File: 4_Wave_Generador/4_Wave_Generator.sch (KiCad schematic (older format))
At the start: 131 parts, among them J10 Jumper, J11 Jumper, J12 Jumper, J13 Jumper, J14 Jumper, J15 Jumper, J4 RESET, J5 Jumper, J6 Jumper, J7 Jumper, J8 Jumper, P1 ECG INPUTS, P10 INPUT_ADC_PIC, P11 DIG_ATMEGA, P12 RG_8421, P13 OUTPUT_DIG_PIC, P14 OUTPUT_TARJET, P15 MUX_S1, P16 DIG_MICRO, P17 SUPPLY_-12V, P18 RS232, P19 I2C, P2 PIC_PROGRAMER, P20 DIG_ATMEGA2, P3 SPI_MICRO, P31 TORNILLO, P32 TORNILLO, P33 TORNILLO, P34 TORNILLO, P35 RS232_PIC, P4 AD8232_CONTROL, P5 OXIMETRO, P6 SUPPLY_12V, P7 SUPPLY_VDD, P8 MCLK_EXTERNAL, P9 SPI_AD9833, SW1 SW_Push, SW2 RESET_PIC, U1 PIC16F688, U2 AD8232_A, U3 ATMEGA328P-AU_MIO, U4 AD9833, U5 LD1117S33TR_MIO, U6 ADG819, U7 ADG819, U8 AD8421, U9 ADG819, Y1 Crystal_8MHz, Y2 XRCHA_16M

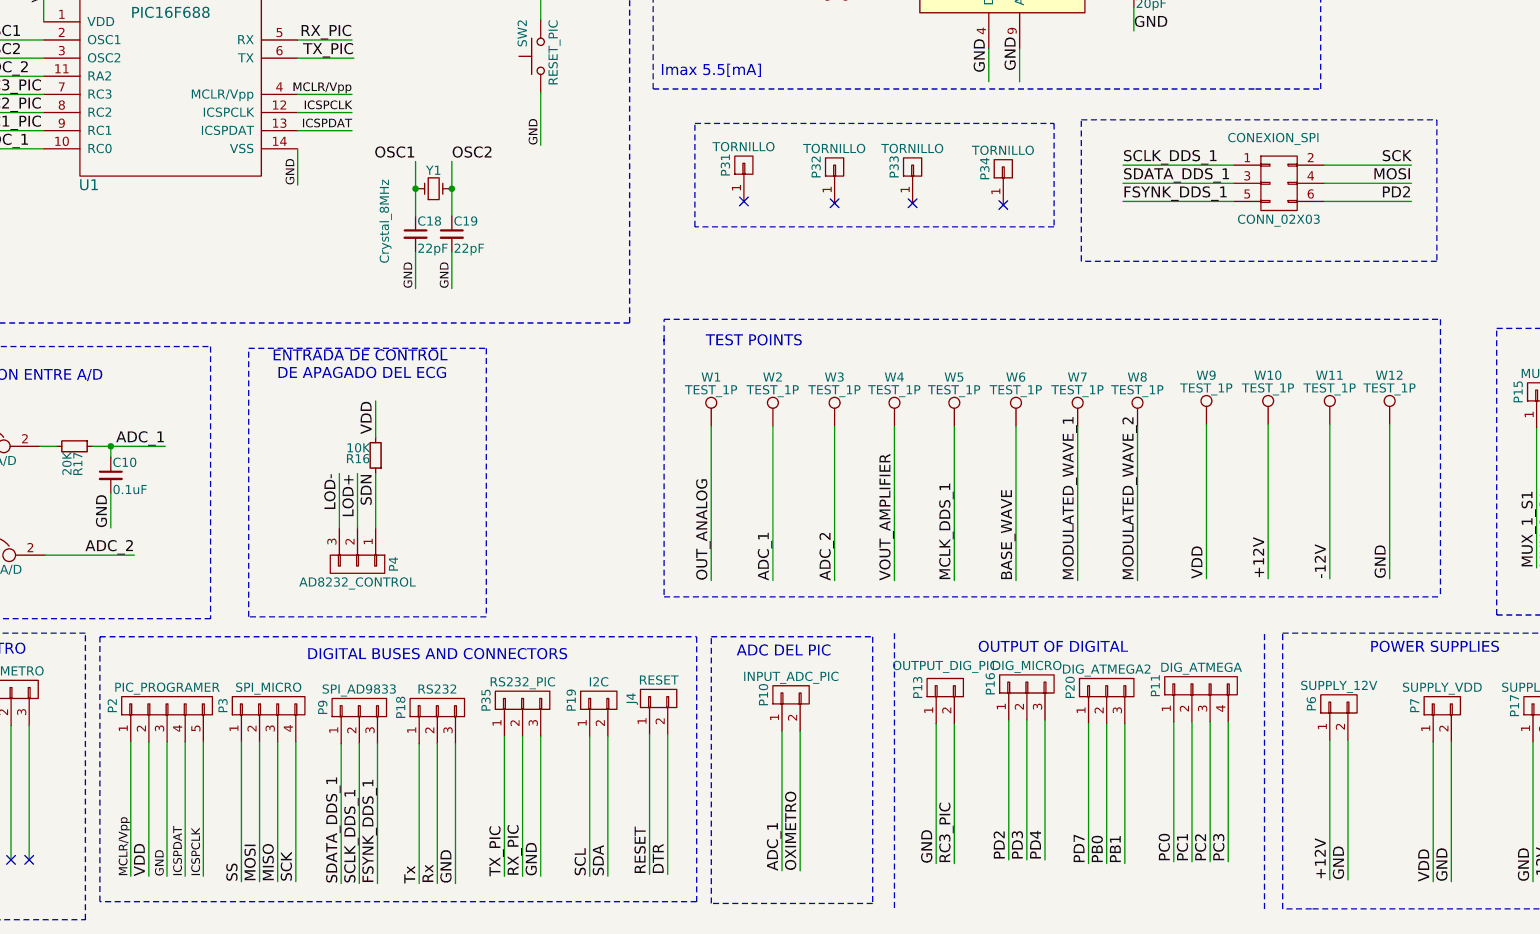
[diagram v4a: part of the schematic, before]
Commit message: GENERADOR V11
TRAZADO DE PISTAS Y VIAS
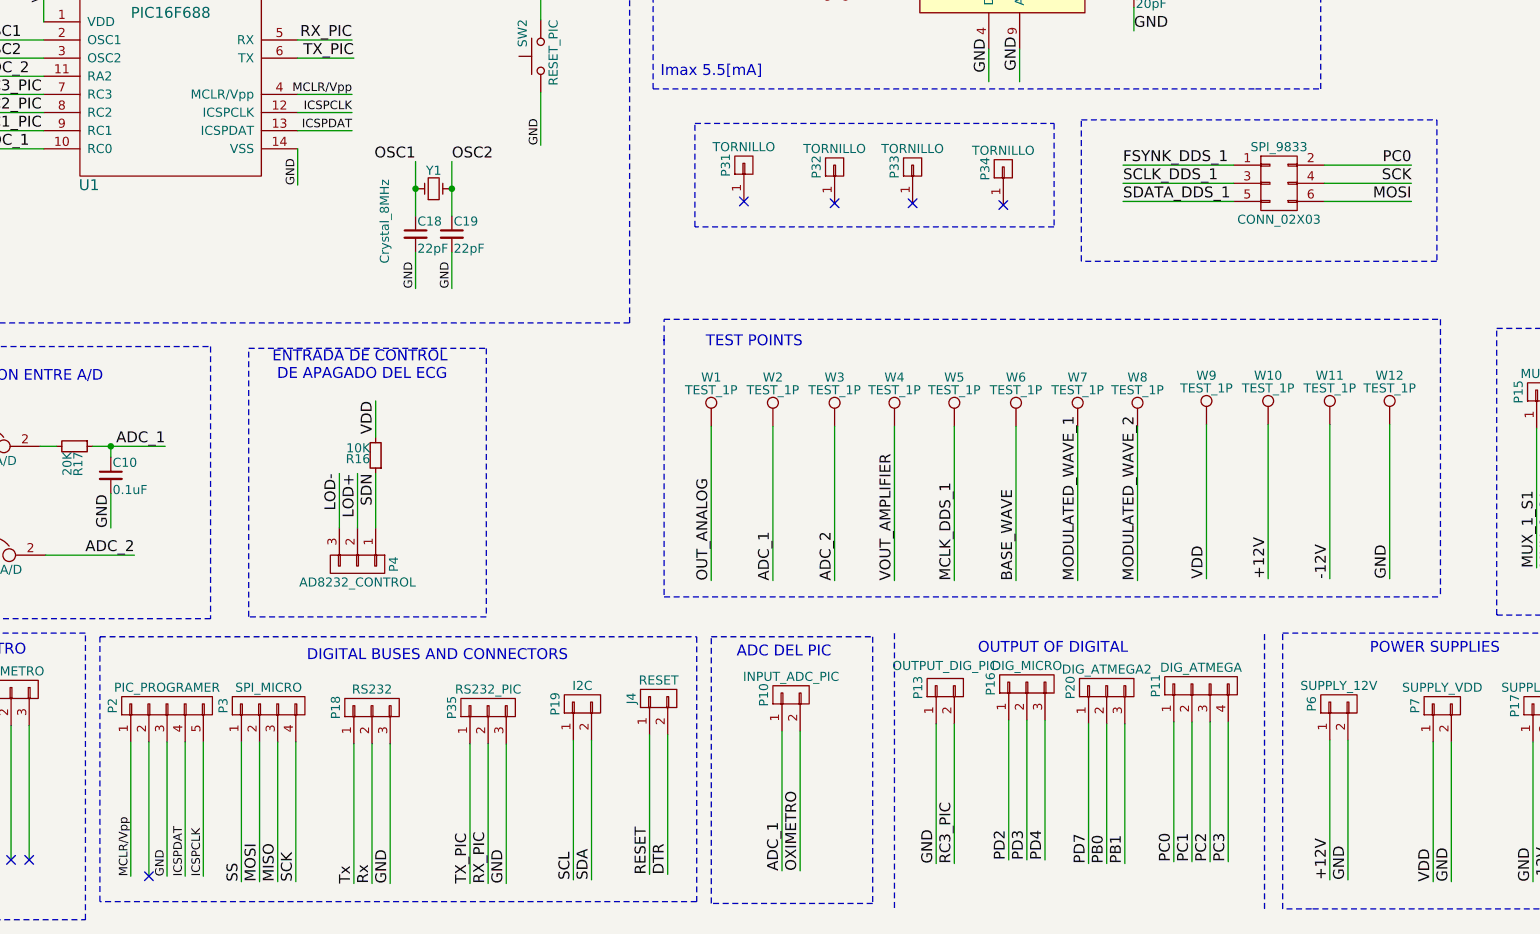
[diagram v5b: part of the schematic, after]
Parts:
- removed CONEXION_SPI: CONN_02X03, Pin_Headers:Pin_Header_Straight_2x03_Pitch2.54mm, symbol CONN_02X03
- removed P9: SPI_AD9833, Foot_Prints_Manager_Outputs:SPI_AD9833, symbol CONN_01X03
- added SPI_9833: CONN_02X03, Foot_Prints_Manager_Outputs:SPI_9833, symbol CONN_02X03
- U5: footprint TO_SOT_Packages_SMD:SOT-223 -> Foot_Prints_Manager_Outputs:SOT-223_este
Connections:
- net FSYNK_DDS_1: now also SPI_9833.1 (P1)
- net MOSI: now also SPI_9833.6 (P6)
- net PC0: now also SPI_9833.2 (P2)
- net SCK: now also SPI_9833.4 (P4)
- net SCLK_DDS_1: now also SPI_9833.3 (P3)
- net SDATA_DDS_1: now also SPI_9833.5 (P5)
- net VDD: no longer P2.2 (P2)
- no-connect marks 15 -> 16
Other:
- moved on the sheet: P18, P19, P35
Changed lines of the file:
@@
 Text Label 3120 10970 1    60   ~ 0
 SCK
-Text Label 3900 10980 1    60   ~ 0
+Text Label 3540 10980 1    60   ~ 0
 Rx
-Text Label 3800 10980 1    60   ~ 0
+Text Label 3440 10980 1    60   ~ 0
 Tx
-Text Label 4000 10980 1    60   ~ 0
+Text Label 3640 10980 1    60   ~ 0
 GND
 Text Notes 3180 9760 0    60   ~ 0
@@
 	0    -1   -1   0
 $EndComp
-Text Label 4840 10940 1    60   ~ 0
+Text Label 4750 10960 1    60   ~ 0
 SDA
-Text Label 4740 10940 1    60   ~ 0
+Text Label 4650 10960 1    60   ~ 0
 SCL
 $Comp
@@
 	1    0    0    -1
 $EndComp
-Text Label 2310 10940 1    60   ~ 0
-VDD
 $Comp
 L PASO_A/D JP1
@@
 Text Label 3440 6430 2    60   ~ 0
 TX_PIC
-Text Label 4270 10940 1    60   ~ 0
+Text Label 4080 10980 1    60   ~ 0
 TX_PIC
-Text Label 4370 10940 1    60   ~ 0
+Text Label 4180 10980 1    60   ~ 0
 RX_PIC
-Text Label 4470 10940 1    60   ~ 0
+Text Label 4280 10980 1    60   ~ 0
 GND
 Text Label 1380 6630 0    60   ~ 0
@@
 $EndComp
 $Comp
-L LD1117S33TR_MIO U5
-U 1 1 59D82649
-P 11050 1080
-F 0 "U5" H 11050 1330 50  0000 C CNN
-F 1 "LD1117S33TR_MIO" H 11050 1280 50  0000 C CNN
-F 2 "TO_SOT_Packages_SMD:SOT-223" H 11050 1180 50  0001 C CNN
-F 3 "" H 11050 1080 50  0001 C CNN
-	1    11050 1080
-	1    0    0    -1
-$EndComp
-$Comp
 L XRCHA_16M Y2
 U 1 1 59DAC6C5
@@
 	3120 10200 3120 10970
 Wire Wire Line
-	3800 10210 3800 10980
-Wire Wire Line
-	3900 10210 3900 10980
-Wire Wire Line
-	4000 10210 4000 10980
+	3440 10210 3440 10980
+Wire Wire Line
+	3540 10210 3540 10980
+Wire Wire Line
+	3640 10210 3640 10980
 Wire Notes Line
 	9700 550  9700 1620
@@
 	12660 2010 12660 550
 Wire Wire Line
-	4740 10170 4740 10940
-Wire Wire Line
-	4840 10170 4840 10940
+	4650 10190 4650 10960
+Wire Wire Line
+	4750 10190 4750 10960
 Wire Wire Line
 	11450 1030 12030 1030
@@
 	3130 6430 3440 6430
 Wire Wire Line
-	4270 10170 4270 10940
-Wire Wire Line
-	4370 10170 4370 10940
-Wire Wire Line
-	4470 10170 4470 10940
+	4080 10210 4080 10980
+Wire Wire Line
+	4180 10210 4180 10980
+Wire Wire Line
+	4280 10210 4280 10980
 Wire Wire Line
 	6650 10100 6650 10870
@@
 Text Notes 5550 9740 0    60   ~ 0
 ADC DEL PIC\n
-$Comp
-L CONN_01X03 P9
-U 1 1 59E0B7ED
-P 3470 10010
-F 0 "P9" H 3470 10210 50  0000 C CNN
-F 1 "SPI_AD9833" V 3570 10010 50  0000 C CNN
-F 2 "Foot_Prints_Manager_Outputs:SPI_AD9833" H 3470 10010 50  0001 C CNN
-F 3 "" H 3470 10010 50  0000 C CNN
-	1    3470 10010
-	0    -1   -1   0
-$EndComp
-Wire Wire Line
-	3370 10210 3370 10980
-Wire Wire Line
-	3470 10210 3470 10980
-Wire Wire Line
-	3570 10210 3570 10980
-Text Label 3370 10980 1    60   ~ 0
-SDATA_DDS_1
-Text Label 3470 10980 1    60   ~ 0
-SCLK_DDS_1
-Text Label 3570 10980 1    60   ~ 0
-FSYNK_DDS_1
 Text Label 6420 9310 1    60   ~ 0
 VOUT_AMPLIFIER
@@
 L CONN_01X03 P18
 U 1 1 59D5CB3B
-P 3900 10010
-F 0 "P18" H 3900 10210 50  0000 C CNN
-F 1 "RS232" V 4000 10010 50  0000 C CNN
-F 2 "Foot_Prints_Manager_Outputs:RS232" H 3900 10010 50  0001 C CNN
-F 3 "" H 3900 10010 50  0000 C CNN
-	1    3900 10010
+P 3540 10010
+F 0 "P18" H 3540 10210 50  0000 C CNN
+F 1 "RS232" V 3640 10010 50  0000 C CNN
+F 2 "Foot_Prints_Manager_Outputs:RS232" H 3540 10010 50  0001 C CNN
+F 3 "" H 3540 10010 50  0000 C CNN
+	1    3540 10010
 	0    -1   -1   0
 $EndComp
@@
 L CONN_01X02 P19
 U 1 1 59D6289E
-P 4790 9970
-F 0 "P19" H 4790 10120 50  0000 C CNN
-F 1 "I2C" V 4890 9970 50  0000 C CNN
-F 2 "Foot_Prints_Manager_Outputs:I2C_2X4" H 4790 9970 50  0001 C CNN
-F 3 "" H 4790 9970 50  0000 C CNN
-	1    4790 9970
+P 4700 9990
+F 0 "P19" H 4700 10140 50  0000 C CNN
+F 1 "I2C" V 4800 9990 50  0000 C CNN
+F 2 "Foot_Prints_Manager_Outputs:I2C_2X4" H 4700 9990 50  0001 C CNN
+F 3 "" H 4700 9990 50  0000 C CNN
+	1    4700 9990
 	0    -1   -1   0
 $EndComp
@@
 L CONN_01X03 P35
 U 1 1 59E4555A
-P 4370 9970
-F 0 "P35" H 4370 10170 50  0000 C CNN
-F 1 "RS232_PIC" V 4470 9970 50  0000 C CNN
-F 2 "Foot_Prints_Manager_Outputs:RS232" H 4370 9970 50  0001 C CNN
-F 3 "" H 4370 9970 50  0000 C CNN
-	1    4370 9970
+P 4180 10010
+F 0 "P35" H 4180 10210 50  0000 C CNN
+F 1 "RS232_PIC" V 4280 10010 50  0000 C CNN
+F 2 "Foot_Prints_Manager_Outputs:RS232" H 4180 10010 50  0001 C CNN
+F 3 "" H 4180 10010 50  0000 C CNN
+	1    4180 10010
 	0    -1   -1   0
 $EndComp
@@
 	0    -1   -1   0
 $EndComp
-$Comp
-L CONN_02X03 CONEXION_SPI
-U 1 1 59D69BA8
+Text Label 7680 7120 0    60   ~ 0
+SCLK_DDS_1
+Text Label 7680 7220 0    60   ~ 0
+SDATA_DDS_1
+Text Label 7680 7020 0    60   ~ 0
+FSYNK_DDS_1
+Wire Wire Line
+	7680 7020 8290 7020
+Wire Wire Line
+	7680 7120 8290 7120
+Wire Wire Line
+	7680 7220 8290 7220
+Wire Wire Line
+	8790 7020 9270 7020
+Wire Wire Line
+	8790 7120 9270 7120
+Wire Wire Line
+	8790 7220 9270 7220
+Text Label 9270 7220 2    60   ~ 0
+MOSI
+Text Label 9270 7120 2    60   ~ 0
+SCK
+Text Label 9270 7020 2    60   ~ 0
+PC0
+Wire Notes Line
+	7450 6770 9410 6770
+Wire Notes Line
+	9410 6770 9410 7550
+Wire Notes Line
+	9410 7550 7450 7550
+Wire Notes Line
+	7450 7550 7450 6770
+$Comp
+L CONN_02X03 SPI_9833
+U 1 1 59DB8D35
 P 8540 7120
-F 0 "CONEXION_SPI" H 8510 7370 50  0000 C CNN
+F 0 "SPI_9833" H 8540 7320 50  0000 C CNN
 F 1 "CONN_02X03" H 8540 6920 50  0000 C CNN
-F 2 "Pin_Headers:Pin_Header_Straight_2x03_Pitch2.54mm" H 8540 5920 50  0001 C CNN
+F 2 "Foot_Prints_Manager_Outputs:SPI_9833" H 8540 5920 50  0001 C CNN
 F 3 "" H 8540 5920 50  0000 C CNN
 	1    8540 7120
 	1    0    0    -1
 $EndComp
-Text Label 7680 7020 0    60   ~ 0
-SCLK_DDS_1
-Text Label 7680 7120 0    60   ~ 0
-SDATA_DDS_1
-Text Label 7680 7220 0    60   ~ 0
-FSYNK_DDS_1
-Wire Wire Line
-	7680 7020 8290 7020
-Wire Wire Line
-	7680 7120 8290 7120
-Wire Wire Line
-	7680 7220 8290 7220
-Wire Wire Line
-	8790 7020 9270 7020
-Wire Wire Line
-	8790 7120 9270 7120
-Wire Wire Line
-	8790 7220 9270 7220
-Text Label 9270 7120 2    60   ~ 0
-MOSI
-Text Label 9270 7020 2    60   ~ 0
-SCK
-Text Label 9270 7220 2    60   ~ 0
-PD2
-Wire Notes Line
-	7450 6770 9410 6770
-Wire Notes Line
-	9410 6770 9410 7550
-Wire Notes Line
-	9410 7550 7450 7550
-Wire Notes Line
-	7450 7550 7450 6770
+NoConn ~ 2310 10940
+$Comp
+L LD1117S33TR_MIO U5
+U 1 1 59D621A9
+P 11050 1080
+F 0 "U5" H 11050 1330 50  0000 C CNN
+F 1 "LD1117S33TR_MIO" H 11050 1280 50  0000 C CNN
+F 2 "Foot_Prints_Manager_Outputs:SOT-223_este" H 11050 1180 50  0001 C CNN
+F 3 "" H 11050 1080 50  0001 C CNN
+	1    11050 1080
+	1    0    0    -1
+$EndComp
 $EndSCHEMATC

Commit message: GENERADOR_V12
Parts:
- removed C21, C29: 8pF, Resistors_SMD:R_0805_HandSoldering, symbol 20pF
- added C11, C12: 8pF, Resistors_SMD:R_0402, symbol 8pF
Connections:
- net GND: now also C11.2, C12.2
- net XTAL1: now also C11.1
- net XTAL2: now also C12.1
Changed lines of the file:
@@
-	1    0    0    -1
-$EndComp
-$Comp
-L 20pF C21
-U 1 1 59D306E8
-P 11820 5270
-F 0 "C21" H 11830 5340 50  0000 L CNN
-F 1 "8pF" H 11830 5190 50  0000 L CNN
-F 2 "Resistors_SMD:R_0805_HandSoldering" H 11730 5240 50  0001 C CNN
-F 3 "" H 11830 5340 50  0001 C CNN
-F 4 "478-3735-2-ND" H 11930 5440 60  0001 C CNN "100V"
-	1    11820 5270
-	1    0    0    -1
-$EndComp
-$Comp
-L 20pF C29
-U 1 1 59D306E9
-P 12620 5270
-F 0 "C29" H 12630 5340 50  0000 L CNN
-F 1 "8pF" H 12630 5190 50  0000 L CNN
-F 2 "Resistors_SMD:R_0805_HandSoldering" H 12530 5240 50  0001 C CNN
-F 3 "" H 12630 5340 50  0001 C CNN
-F 4 "478-3735-2-ND" H 12730 5440 60  0001 C CNN "100V"
-	1    12620 5270
 	1    0    0    -1
 $EndComp
@@
 	1    0    0    -1
 $EndComp
+$Comp
+L 8pF C11
+U 1 1 59D678F9
+P 11820 5270
+F 0 "C11" H 11830 5340 50  0000 L CNN
+F 1 "8pF" H 11830 5190 50  0000 L CNN
+F 2 "Resistors_SMD:R_0402" H 11730 5240 50  0001 C CNN
+F 3 "" H 11830 5340 50  0000 C CNN
+F 4 "399-1113-2-ND" H 11930 5440 39  0001 C CNN "CAP CER 22PF 50V C0G/NP0 0805"
+	1    11820 5270
+	1    0    0    -1
+$EndComp
+$Comp
+L 8pF C12
+U 1 1 59D6945B
+P 12620 5270
+F 0 "C12" H 12630 5340 50  0000 L CNN
+F 1 "8pF" H 12630 5190 50  0000 L CNN
+F 2 "Resistors_SMD:R_0402" H 12530 5240 50  0001 C CNN
+F 3 "" H 12630 5340 50  0000 C CNN
+F 4 "399-1113-2-ND" H 12730 5440 39  0001 C CNN "CAP CER 22PF 50V C0G/NP0 0805"
+	1    12620 5270
+	1    0    0    -1
+$EndComp
